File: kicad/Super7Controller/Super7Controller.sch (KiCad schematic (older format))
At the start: 28 parts, among them CON1 AVR-ISP-6, IC1 ATMEGA328P-P, IC2 74HC238, P3 CONN_01X13, P4 CONN_01X09, P5 UART, P6 CONN_01X02, P7 CONN_01X02, U1 ULN2003A

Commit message: DC6 is gone
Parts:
- U1: symbol ULN2003A -> ULN2003A-RESCUE-Super7Controller
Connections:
- net labels removed: DC_6
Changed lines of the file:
@@
 EESchema Schematic File Version 2
+LIBS:Super7Controller-rescue
 LIBS:power
 LIBS:device
@@
 Text GLabel 11350 2150 1    50   Input ~ 0
 DC_5
-Text GLabel 11450 2150 1    50   Input ~ 0
-DC_6
 $Comp
 L CONN_01X13 P3
@@
 NoConn ~ 8650 4100
 $Comp
-L ULN2003A U1
+L ULN2003A-RESCUE-Super7Controller U1
 U 1 1 586AB8C8
 P 12100 4050
@@
 Text GLabel 12750 4050 2    60   Input ~ 0
 DC_5
-Text GLabel 12750 4150 2    60   Input ~ 0
-DC_6
 NoConn ~ 12750 4450
 NoConn ~ 12750 4250

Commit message: delete all the old parts I won't use
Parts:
- removed C1, C2: 0.1uF, Capacitors_ThroughHole:C_Disc_D3_P2.5, symbol C_Small
- removed CON1: AVR-ISP-6, footprints:ICSP, symbol AVR-ISP-6
- removed IC1: ATMEGA328P-P, footprints:DIP28, symbol ATMEGA328P-P
- removed P5: UART, misc:Strip_1x06, symbol CONN_01X06
- removed P6, P7: CONN_01X02, misc:Strip_1x02, symbol CONN_01X02
- removed R17: 10k, footprints:0.125_Resistor, symbol R
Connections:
- net labels removed: MISO, MOSI, PC6, RESET, RX, SCK, TX
- wire segments 76 -> 56
- no-connect marks 4 -> 5

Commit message: connect ESP dev board on schematic
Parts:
- removed IC2: 74HC238, Housings_DIP:DIP-16_W7.62mm, symbol 74HC238
- added U?: HiLetgo_ESP-WROOM-32_Development_Board, symbol HiLetgo_ESP-WROOM-32_Development_Board
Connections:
- net labels added: DC_6
- net labels removed: DC_A, DC_B, DC_C
- wire segments 56 -> 69
- no-connect marks 5 -> 2
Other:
- moved on the sheet: R1, R10, R11, R12, R13, R14, R15, R16, R2, R3, R4, R5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

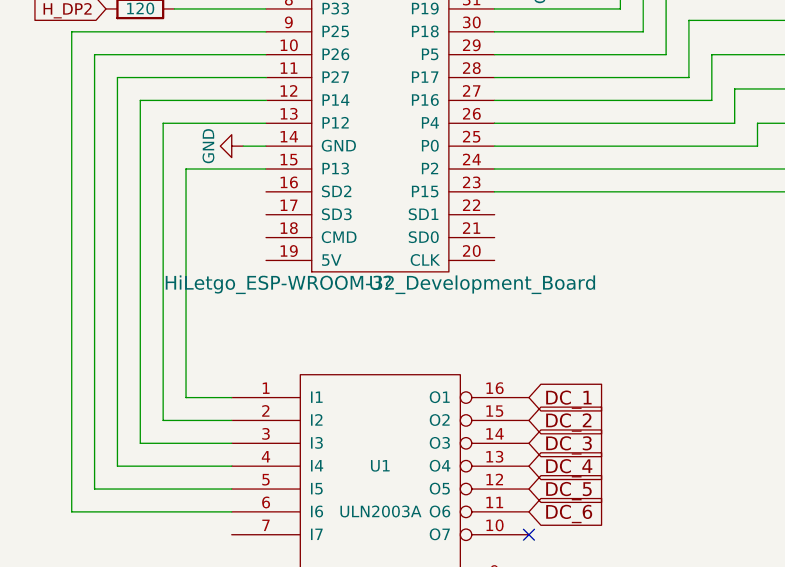
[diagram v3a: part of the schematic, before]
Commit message: change resistors to surface mount
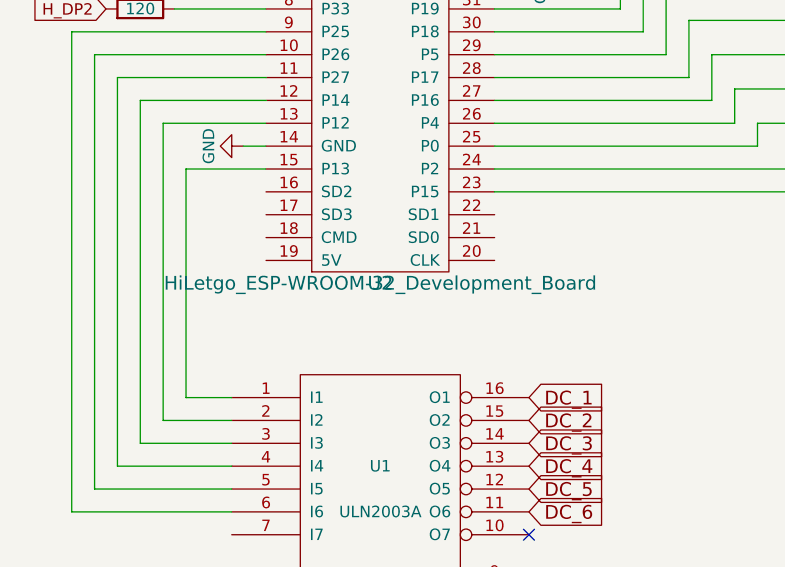
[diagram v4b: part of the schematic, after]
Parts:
- R1, R10, R11, R12, R13, R14, R15, R16, R2, R3, R4, R5, R6, R7, R8, R9: footprint footprints:0.125_Resistor -> Resistors_SMD:R_0805_HandSoldering
- gave numbers to parts that had none: 1
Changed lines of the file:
@@
 F 0 "R12" V 9480 1500 50  0000 C CNN
 F 1 "120" V 9400 1500 50  0000 C CNN
-F 2 "footprints:0.125_Resistor" V 9330 1500 50  0001 C CNN
+F 2 "Resistors_SMD:R_0805_HandSoldering" V 9330 1500 50  0001 C CNN
 F 3 "" H 9400 1500 50  0000 C CNN
 	1    9400 1500
@@
 F 0 "R13" V 9480 1650 50  0000 C CNN
 F 1 "120" V 9400 1650 50  0000 C CNN
-F 2 "footprints:0.125_Resistor" V 9330 1650 50  0001 C CNN
+F 2 "Resistors_SMD:R_0805_HandSoldering" V 9330 1650 50  0001 C CNN
 F 3 "" H 9400 1650 50  0000 C CNN
 	1    9400 1650
@@
 F 0 "R3" V 9480 1800 50  0000 C CNN
 F 1 "120" V 9400 1800 50  0000 C CNN
-F 2 "footprints:0.125_Resistor" V 9330 1800 50  0001 C CNN
+F 2 "Resistors_SMD:R_0805_HandSoldering" V 9330 1800 50  0001 C CNN
 F 3 "" H 9400 1800 50  0000 C CNN
 	1    9400 1800
@@
 F 0 "R2" V 9480 1950 50  0000 C CNN
 F 1 "120" V 9400 1950 50  0000 C CNN
-F 2 "footprints:0.125_Resistor" V 9330 1950 50  0001 C CNN
+F 2 "Resistors_SMD:R_0805_HandSoldering" V 9330 1950 50  0001 C CNN
 F 3 "" H 9400 1950 50  0000 C CNN
 	1    9400 1950
@@
 F 0 "R1" V 9480 2100 50  0000 C CNN
 F 1 "120" V 9400 2100 50  0000 C CNN
-F 2 "footprints:0.125_Resistor" V 9330 2100 50  0001 C CNN
+F 2 "Resistors_SMD:R_0805_HandSoldering" V 9330 2100 50  0001 C CNN
 F 3 "" H 9400 2100 50  0000 C CNN
 	1    9400 2100
@@
 F 0 "R10" V 9480 2250 50  0000 C CNN
 F 1 "120" V 9400 2250 50  0000 C CNN
-F 2 "footprints:0.125_Resistor" V 9330 2250 50  0001 C CNN
+F 2 "Resistors_SMD:R_0805_HandSoldering" V 9330 2250 50  0001 C CNN
 F 3 "" H 9400 2250 50  0000 C CNN
 	1    9400 2250
@@
 F 0 "R11" V 9480 2400 50  0000 C CNN
 F 1 "120" V 9400 2400 50  0000 C CNN
-F 2 "footprints:0.125_Resistor" V 9330 2400 50  0001 C CNN
+F 2 "Resistors_SMD:R_0805_HandSoldering" V 9330 2400 50  0001 C CNN
 F 3 "" H 9400 2400 50  0000 C CNN
 	1    9400 2400
@@
 F 0 "R4" V 9480 2550 50  0000 C CNN
 F 1 "120" V 9400 2550 50  0000 C CNN
-F 2 "footprints:0.125_Resistor" V 9330 2550 50  0001 C CNN
+F 2 "Resistors_SMD:R_0805_HandSoldering" V 9330 2550 50  0001 C CNN
 F 3 "" H 9400 2550 50  0000 C CNN
 	1    9400 2550
@@
 F 0 "R15" V 9480 2700 50  0000 C CNN
 F 1 "120" V 9400 2700 50  0000 C CNN
-F 2 "footprints:0.125_Resistor" V 9330 2700 50  0001 C CNN
+F 2 "Resistors_SMD:R_0805_HandSoldering" V 9330 2700 50  0001 C CNN
 F 3 "" H 9400 2700 50  0000 C CNN
 	1    9400 2700
@@
 F 0 "R16" V 9480 2850 50  0000 C CNN
 F 1 "120" V 9400 2850 50  0000 C CNN
-F 2 "footprints:0.125_Resistor" V 9330 2850 50  0001 C CNN
+F 2 "Resistors_SMD:R_0805_HandSoldering" V 9330 2850 50  0001 C CNN
 F 3 "" H 9400 2850 50  0000 C CNN
 	1    9400 2850
@@
 F 0 "R8" V 9480 3000 50  0000 C CNN
 F 1 "120" V 9400 3000 50  0000 C CNN
-F 2 "footprints:0.125_Resistor" V 9330 3000 50  0001 C CNN
+F 2 "Resistors_SMD:R_0805_HandSoldering" V 9330 3000 50  0001 C CNN
 F 3 "" H 9400 3000 50  0000 C CNN
 	1    9400 3000
@@
 F 0 "R6" V 9480 3150 50  0000 C CNN
 F 1 "120" V 9400 3150 50  0000 C CNN
-F 2 "footprints:0.125_Resistor" V 9330 3150 50  0001 C CNN
+F 2 "Resistors_SMD:R_0805_HandSoldering" V 9330 3150 50  0001 C CNN
 F 3 "" H 9400 3150 50  0000 C CNN
 	1    9400 3150
@@
 F 0 "R5" V 6330 1900 50  0000 C CNN
 F 1 "120" V 6250 1900 50  0000 C CNN
-F 2 "footprints:0.125_Resistor" V 6180 1900 50  0001 C CNN
+F 2 "Resistors_SMD:R_0805_HandSoldering" V 6180 1900 50  0001 C CNN
 F 3 "" H 6250 1900 50  0000 C CNN
 	1    6250 1900
@@
 F 0 "R14" V 6330 2050 50  0000 C CNN
 F 1 "120" V 6250 2050 50  0000 C CNN
-F 2 "footprints:0.125_Resistor" V 6180 2050 50  0001 C CNN
+F 2 "Resistors_SMD:R_0805_HandSoldering" V 6180 2050 50  0001 C CNN
 F 3 "" H 6250 2050 50  0000 C CNN
 	1    6250 2050
@@
 F 0 "R7" V 6330 2200 50  0000 C CNN
 F 1 "120" V 6250 2200 50  0000 C CNN
-F 2 "footprints:0.125_Resistor" V 6180 2200 50  0001 C CNN
+F 2 "Resistors_SMD:R_0805_HandSoldering" V 6180 2200 50  0001 C CNN
 F 3 "" H 6250 2200 50  0000 C CNN
 	1    6250 2200
@@
 F 0 "R9" V 6330 2350 50  0000 C CNN
 F 1 "120" V 6250 2350 50  0000 C CNN
-F 2 "footprints:0.125_Resistor" V 6180 2350 50  0001 C CNN
+F 2 "Resistors_SMD:R_0805_HandSoldering" V 6180 2350 50  0001 C CNN
 F 3 "" H 6250 2350 50  0000 C CNN
 	1    6250 2350
@@
 $EndComp
 $Comp
-L VCC #PWR01
+L VCC #PWR1
 U 1 1 585DF033
 P 6700 1600
-F 0 "#PWR01" H 6700 1450 50  0001 C CNN
+F 0 "#PWR1" H 6700 1450 50  0001 C CNN
 F 1 "VCC" H 6700 1750 50  0000 C CNN
 F 2 "" H 6700 1600 50  0000 C CNN
@@
 $EndComp
 $Comp
-L GND #PWR03
+L GND #PWR2
 U 1 1 585DF7E3
 P 6700 2950
-F 0 "#PWR03" H 6700 2700 50  0001 C CNN
+F 0 "#PWR2" H 6700 2700 50  0001 C CNN
 F 1 "GND" H 6700 2800 50  0000 C CNN
 F 2 "" H 6700 2950 50  0000 C CNN
@@
 $EndComp
 $Comp
-L PWR_FLAG #FLG06
+L PWR_FLAG #FLG1
 U 1 1 585EE745
 P 10500 1400
-F 0 "#FLG06" H 10500 1495 50  0001 C CNN
+F 0 "#FLG1" H 10500 1495 50  0001 C CNN
 F 1 "PWR_FLAG" H 10500 1580 50  0000 C CNN
 F 2 "" H 10500 1400 50  0000 C CNN
@@
 $EndComp
 $Comp
-L GND #PWR07
+L GND #PWR5
 U 1 1 585EEC8B
 P 10500 1450
-F 0 "#PWR07" H 10500 1200 50  0001 C CNN
+F 0 "#PWR5" H 10500 1200 50  0001 C CNN
 F 1 "GND" H 10500 1300 50  0000 C CNN
 F 2 "" H 10500 1450 50  0000 C CNN
@@
 $EndComp
 $Comp
-L VCC #PWR08
+L VCC #PWR6
 U 1 1 585EED05
 P 10950 1450
-F 0 "#PWR08" H 10950 1300 50  0001 C CNN
+F 0 "#PWR6" H 10950 1300 50  0001 C CNN
 F 1 "VCC" H 10950 1600 50  0000 C CNN
 F 2 "" H 10950 1450 50  0000 C CNN
@@
 $EndComp
 $Comp
-L PWR_FLAG #FLG09
+L PWR_FLAG #FLG2
 U 1 1 585EED7F
 P 10950 1400
-F 0 "#FLG09" H 10950 1495 50  0001 C CNN
+F 0 "#FLG2" H 10950 1495 50  0001 C CNN
 F 1 "PWR_FLAG" H 10950 1580 50  0000 C CNN
 F 2 "" H 10950 1400 50  0000 C CNN
@@
 NoConn ~ 7950 4650
 $Comp
-L HiLetgo_ESP-WROOM-32_Development_Board U?
+L HiLetgo_ESP-WROOM-32_Development_Board U2
 U 1 1 5A71DF56
 P 7300 3550
-F 0 "U?" H 7300 3550 60  0000 C CNN
+F 0 "U2" H 7300 3550 60  0000 C CNN
 F 1 "HiLetgo_ESP-WROOM-32_Development_Board" H 7300 3550 60  0000 C CNN
 F 2 "" H 7300 3550 60  0001 C CNN
@@
 	6700 1650 6700 1600
 $Comp
-L GND #PWR?
+L GND #PWR3
 U 1 1 5A71E497
 P 7850 1650
-F 0 "#PWR?" H 7850 1400 50  0001 C CNN
+F 0 "#PWR3" H 7850 1400 50  0001 C CNN
 F 1 "GND" H 7850 1500 50  0000 C CNN
 F 2 "" H 7850 1650 50  0000 C CNN
@@
 $EndComp
 $Comp
-L GND #PWR?
+L GND #PWR4
 U 1 1 5A71E4E1
 P 7850 2250
-F 0 "#PWR?" H 7850 2000 50  0001 C CNN
+F 0 "#PWR4" H 7850 2000 50  0001 C CNN
 F 1 "GND" H 7850 2100 50  0000 C CNN
 F 2 "" H 7850 2250 50  0000 C CNN

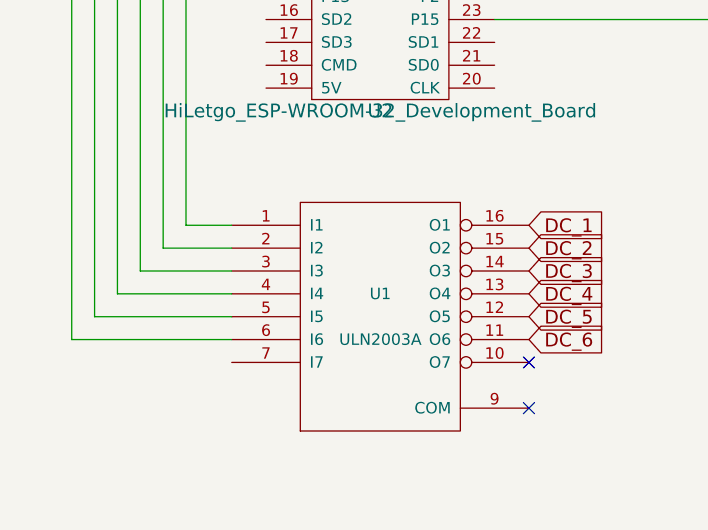
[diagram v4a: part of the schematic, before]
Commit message: use old symbol for ULN2003A because GND is needed
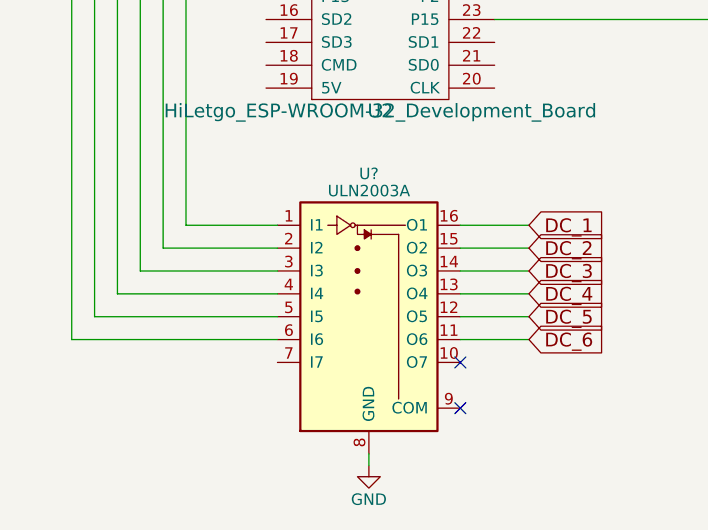
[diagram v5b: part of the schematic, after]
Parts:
- removed U1: ULN2003A, Housings_DIP:DIP-16_W7.62mm, symbol ULN2003A-RESCUE-Super7Controller
- added U?: ULN2003A, symbol ULN2003A
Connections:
- net DC_1: now also U?.16 (O1)
- net DC_2: now also U?.15 (O2)
- net DC_3: now also U?.14 (O3)
- net DC_4: now also U?.13 (O4)
- net DC_5: now also U?.12 (O5)
- net DC_6: now also U?.11 (O6)
- net GND: now also U?.8 (GND)
- net at U2.15 (P13): now also U?.1 (I1)
- net at U2.13 (P12): now also U?.2 (I2)
- net at U2.12 (P14): now also U?.3 (I3)
- net at U2.11 (P27): now also U?.4 (I4)
- net at U2.10 (P26): now also U?.5 (I5)
- net at U2.9 (P25): now also U?.6 (I6)
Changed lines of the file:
@@
 	0    -1   -1   0
-$EndComp
-$Comp
-L ULN2003A-RESCUE-Super7Controller U1
-U 1 1 586AB8C8
-P 7300 4450
-F 0 "U1" H 7300 4550 50  0000 C CNN
-F 1 "ULN2003A" H 7300 4350 50  0000 C CNN
-F 2 "Housings_DIP:DIP-16_W7.62mm" H 7300 4450 50  0001 C CNN
-F 3 "" H 7300 4450 50  0000 C CNN
-	1    7300 4450
-	1    0    0    -1
 $EndComp
 Text GLabel 7950 4050 2    60   Input ~ 0
@@
 Text GLabel 7950 4450 2    60   Input ~ 0
 DC_5
-NoConn ~ 7950 4850
-NoConn ~ 7950 4650
+NoConn ~ 7650 4850
+NoConn ~ 7650 4650
 $Comp
 L HiLetgo_ESP-WROOM-32_Development_Board U2
@@
 	9100 3050 9100 3000
 Wire Wire Line
-	6650 4050 6450 4050
+	6450 4050 6850 4050
 Wire Wire Line
 	6450 4050 6450 3050
@@
 	6450 3050 6800 3050
 Wire Wire Line
-	6650 4150 6350 4150
+	6350 4150 6850 4150
 Wire Wire Line
 	6350 4150 6350 2850
@@
 	6350 2850 6800 2850
 Wire Wire Line
-	6650 4250 6250 4250
+	6250 4250 6850 4250
 Wire Wire Line
 	6250 4250 6250 2750
@@
 	6250 2750 6800 2750
 Wire Wire Line
-	6650 4350 6150 4350
+	6150 4350 6850 4350
 Wire Wire Line
 	6150 4350 6150 2650
@@
 	6150 2650 6800 2650
 Wire Wire Line
-	6650 4450 6050 4450
+	6050 4450 6850 4450
 Wire Wire Line
 	6050 4450 6050 2550
@@
 	5950 2450 5950 4550
 Wire Wire Line
-	5950 4550 6650 4550
+	5950 4550 6850 4550
 Text GLabel 7950 4550 2    60   Input ~ 0
 DC_6
@@
 Wire Wire Line
 	6800 2350 6400 2350
+$Comp
+L ULN2003A U?
+U 1 1 5A72257F
+P 7250 4350
+F 0 "U?" H 7250 4875 50  0000 C CNN
+F 1 "ULN2003A" H 7250 4800 50  0000 C CNN
+F 2 "" H 7300 3700 50  0001 L CNN
+F 3 "" H 7350 4250 50  0001 C CNN
+	1    7250 4350
+	1    0    0    -1
+$EndComp
+Wire Wire Line
+	7950 4050 7650 4050
+Wire Wire Line
+	7650 4150 7950 4150
+Wire Wire Line
+	7950 4250 7650 4250
+Wire Wire Line
+	7650 4350 7950 4350
+Wire Wire Line
+	7950 4450 7650 4450
+Wire Wire Line
+	7650 4550 7950 4550
+$Comp
+L GND #PWR?
+U 1 1 5A722BDF
+P 7250 5100
+F 0 "#PWR?" H 7250 4850 50  0001 C CNN
+F 1 "GND" H 7250 4950 50  0000 C CNN
+F 2 "" H 7250 5100 50  0000 C CNN
+F 3 "" H 7250 5100 50  0000 C CNN
+	1    7250 5100
+	1    0    0    -1
+$EndComp
+Wire Wire Line
+	7250 5050 7250 5100
 $EndSCHEMATC

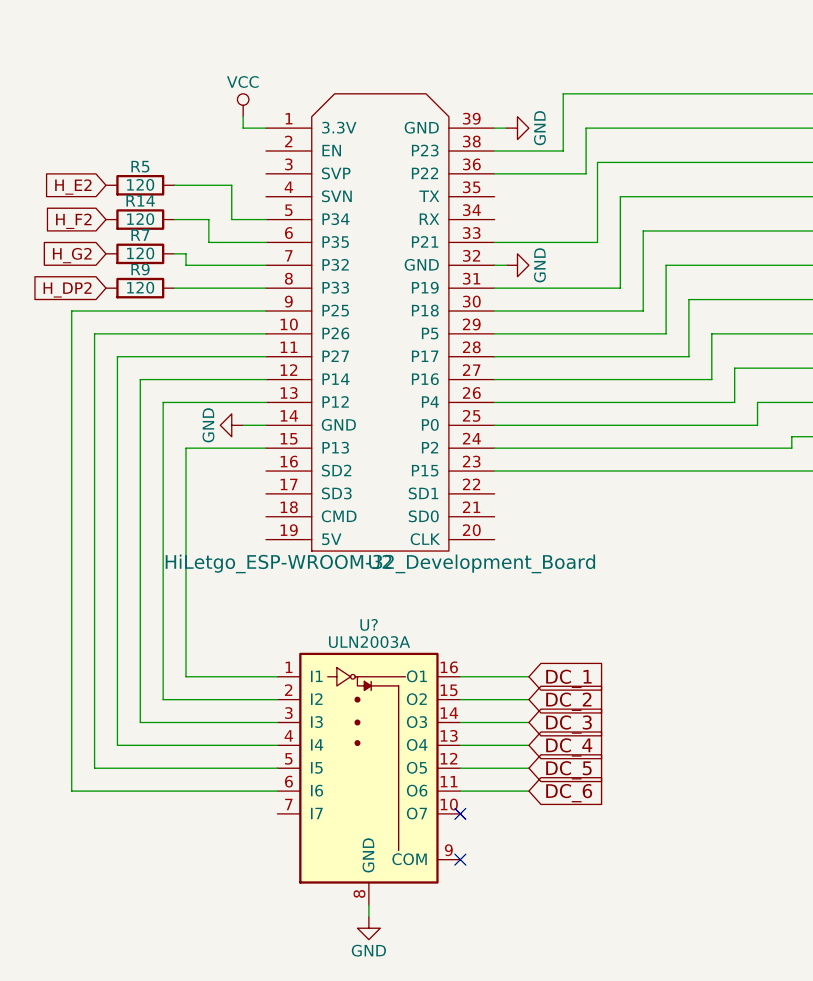
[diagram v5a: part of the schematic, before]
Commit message: change ESP pins to bidirectional to pass ERC
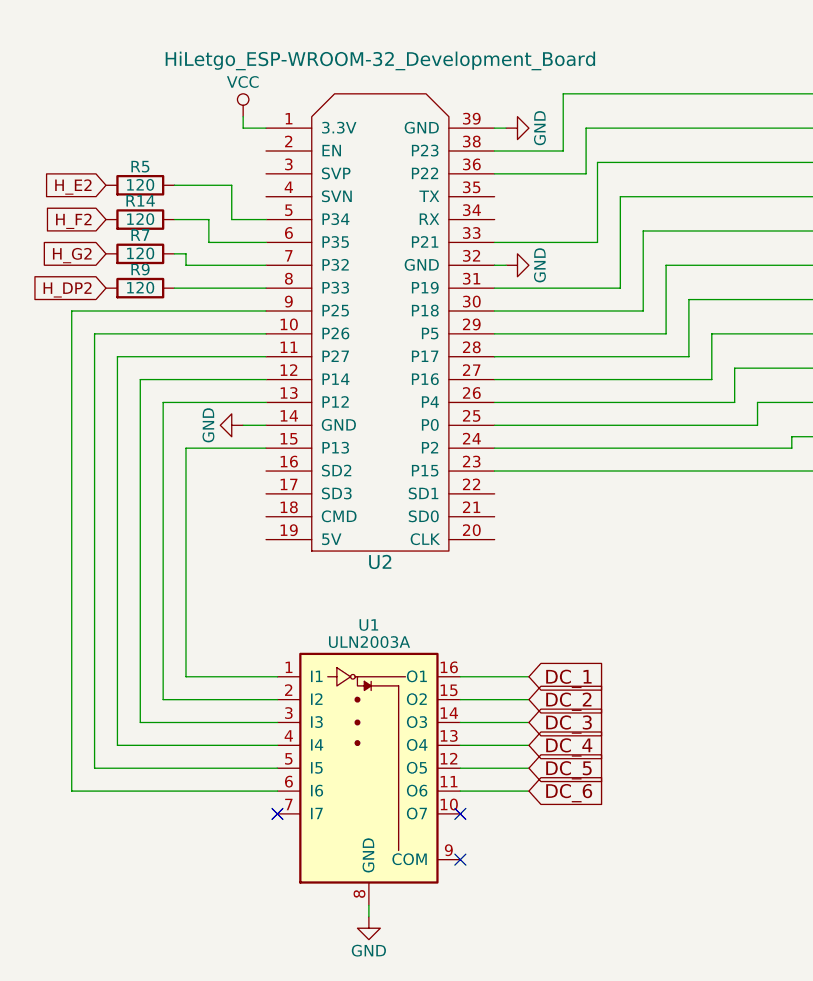
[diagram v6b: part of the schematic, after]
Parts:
- gave numbers to parts that had none: 1
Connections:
- no-connect marks 2 -> 3
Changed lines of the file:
@@
 $EndComp
 $Comp
-L VCC #PWR1
+L VCC #PWR01
 U 1 1 585DF033
 P 6700 1600
-F 0 "#PWR1" H 6700 1450 50  0001 C CNN
+F 0 "#PWR01" H 6700 1450 50  0001 C CNN
 F 1 "VCC" H 6700 1750 50  0000 C CNN
 F 2 "" H 6700 1600 50  0000 C CNN
@@
 $EndComp
 $Comp
-L GND #PWR2
+L GND #PWR02
 U 1 1 585DF7E3
 P 6700 2950
-F 0 "#PWR2" H 6700 2700 50  0001 C CNN
+F 0 "#PWR02" H 6700 2700 50  0001 C CNN
 F 1 "GND" H 6700 2800 50  0000 C CNN
 F 2 "" H 6700 2950 50  0000 C CNN
@@
 $EndComp
 $Comp
-L PWR_FLAG #FLG1
+L PWR_FLAG #FLG03
 U 1 1 585EE745
 P 10500 1400
-F 0 "#FLG1" H 10500 1495 50  0001 C CNN
+F 0 "#FLG03" H 10500 1495 50  0001 C CNN
 F 1 "PWR_FLAG" H 10500 1580 50  0000 C CNN
 F 2 "" H 10500 1400 50  0000 C CNN
@@
 $EndComp
 $Comp
-L GND #PWR5
+L GND #PWR04
 U 1 1 585EEC8B
 P 10500 1450
-F 0 "#PWR5" H 10500 1200 50  0001 C CNN
+F 0 "#PWR04" H 10500 1200 50  0001 C CNN
 F 1 "GND" H 10500 1300 50  0000 C CNN
 F 2 "" H 10500 1450 50  0000 C CNN
@@
 $EndComp
 $Comp
-L VCC #PWR6
+L VCC #PWR05
 U 1 1 585EED05
 P 10950 1450
-F 0 "#PWR6" H 10950 1300 50  0001 C CNN
+F 0 "#PWR05" H 10950 1300 50  0001 C CNN
 F 1 "VCC" H 10950 1600 50  0000 C CNN
 F 2 "" H 10950 1450 50  0000 C CNN
@@
 $EndComp
 $Comp
-L PWR_FLAG #FLG2
+L PWR_FLAG #FLG06
 U 1 1 585EED7F
 P 10950 1400
-F 0 "#FLG2" H 10950 1495 50  0001 C CNN
+F 0 "#FLG06" H 10950 1495 50  0001 C CNN
 F 1 "PWR_FLAG" H 10950 1580 50  0000 C CNN
 F 2 "" H 10950 1400 50  0000 C CNN
@@
 P 7300 3550
 F 0 "U2" H 7300 3550 60  0000 C CNN
-F 1 "HiLetgo_ESP-WROOM-32_Development_Board" H 7300 3550 60  0000 C CNN
+F 1 "HiLetgo_ESP-WROOM-32_Development_Board" H 7300 5750 60  0000 C CNN
 F 2 "" H 7300 3550 60  0001 C CNN
 F 3 "" H 7300 3550 60  0001 C CNN
@@
 	6700 1650 6700 1600
 $Comp
-L GND #PWR3
+L GND #PWR07
 U 1 1 5A71E497
 P 7850 1650
-F 0 "#PWR3" H 7850 1400 50  0001 C CNN
+F 0 "#PWR07" H 7850 1400 50  0001 C CNN
 F 1 "GND" H 7850 1500 50  0000 C CNN
 F 2 "" H 7850 1650 50  0000 C CNN
@@
 $EndComp
 $Comp
-L GND #PWR4
+L GND #PWR08
 U 1 1 5A71E4E1
 P 7850 2250
-F 0 "#PWR4" H 7850 2000 50  0001 C CNN
+F 0 "#PWR08" H 7850 2000 50  0001 C CNN
 F 1 "GND" H 7850 2100 50  0000 C CNN
 F 2 "" H 7850 2250 50  0000 C CNN
@@
 	6800 2350 6400 2350
 $Comp
-L ULN2003A U?
+L ULN2003A U1
 U 1 1 5A72257F
 P 7250 4350
-F 0 "U?" H 7250 4875 50  0000 C CNN
+F 0 "U1" H 7250 4875 50  0000 C CNN
 F 1 "ULN2003A" H 7250 4800 50  0000 C CNN
 F 2 "" H 7300 3700 50  0001 L CNN
@@
 	7650 4550 7950 4550
 $Comp
-L GND #PWR?
+L GND #PWR09
 U 1 1 5A722BDF
 P 7250 5100
-F 0 "#PWR?" H 7250 4850 50  0001 C CNN
+F 0 "#PWR09" H 7250 4850 50  0001 C CNN
 F 1 "GND" H 7250 4950 50  0000 C CNN
 F 2 "" H 7250 5100 50  0000 C CNN
@@
 Wire Wire Line
 	7250 5050 7250 5100
+NoConn ~ 6850 4650
 $EndSCHEMATC

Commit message: use SOIC footprint for ULN
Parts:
- U1: footprint (none) -> Housings_SOIC:SOIC-16_3.9x9.9mm_Pitch1.27mm
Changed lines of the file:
@@
 F 0 "U1" H 7250 4875 50  0000 C CNN
 F 1 "ULN2003A" H 7250 4800 50  0000 C CNN
-F 2 "" H 7300 3700 50  0001 L CNN
+F 2 "Housings_SOIC:SOIC-16_3.9x9.9mm_Pitch1.27mm" H 7300 3700 50  0001 L CNN
 F 3 "" H 7350 4250 50  0001 C CNN
 	1    7250 4350

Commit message: assign esp32 footprint to schematic symbol
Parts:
- U2: footprint (none) -> hiletgo_esp-wroom-32_development_board:hiletgo_esp-wroom-32_development_board
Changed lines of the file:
@@
 F 0 "U2" H 7300 3550 60  0000 C CNN
 F 1 "HiLetgo_ESP-WROOM-32_Development_Board" H 7300 5750 60  0000 C CNN
-F 2 "" H 7300 3550 60  0001 C CNN
+F 2 "hiletgo_esp-wroom-32_development_board:hiletgo_esp-wroom-32_development_board" H 7300 3550 60  0001 C CNN
 F 3 "" H 7300 3550 60  0001 C CNN
 	1    7300 3550
